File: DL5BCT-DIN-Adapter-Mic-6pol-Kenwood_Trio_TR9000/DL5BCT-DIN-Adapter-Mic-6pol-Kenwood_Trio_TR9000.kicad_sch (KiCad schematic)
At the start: 3 parts, among them J1 DIN-5_180degree, J2 GX16-6_Radio_Microphone-6-pol, J3 3.5 mm Audio Plug

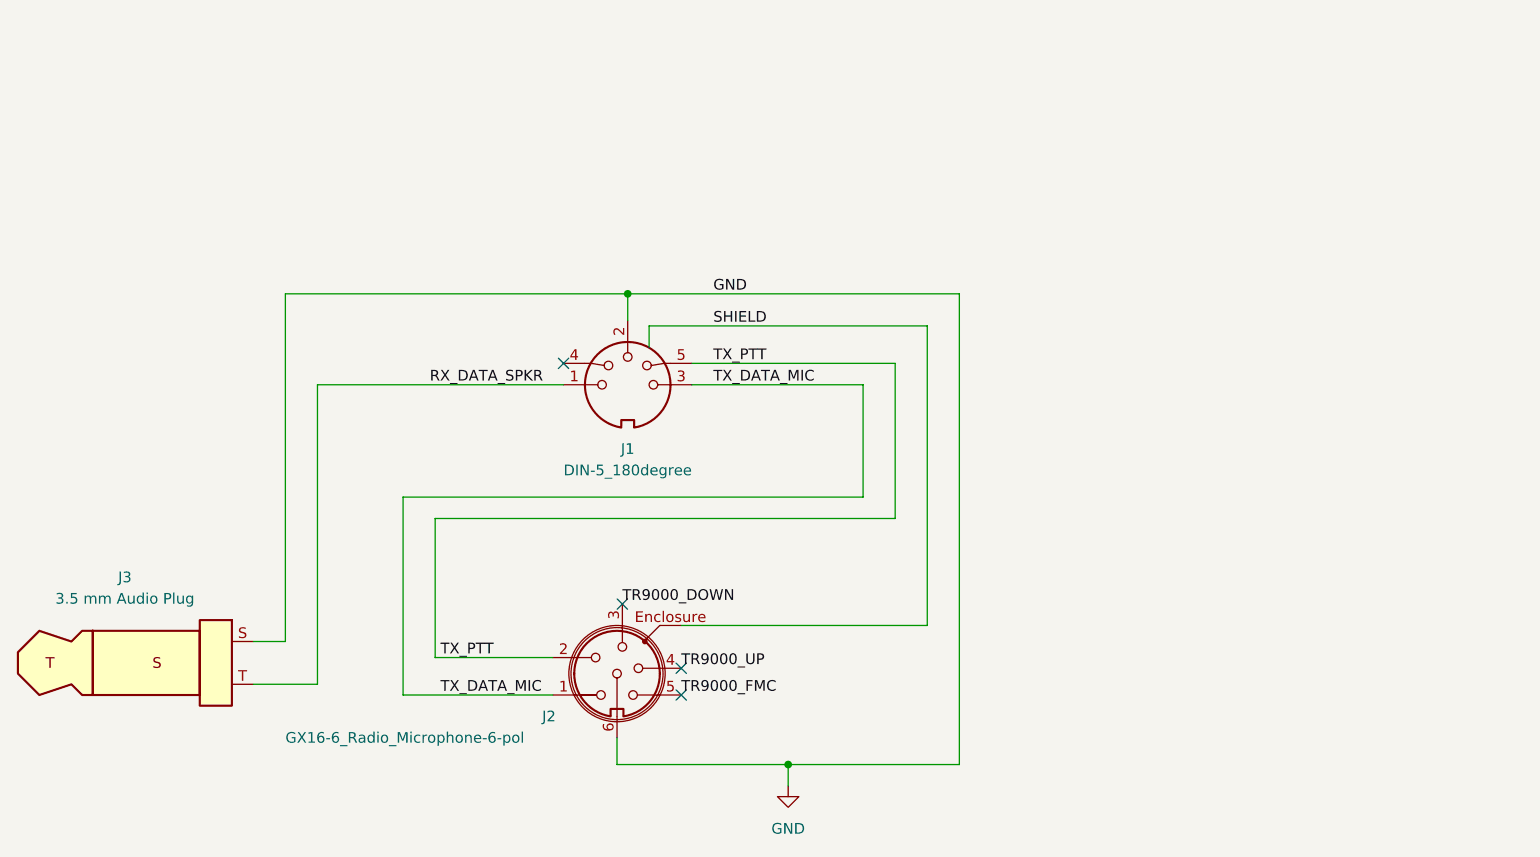
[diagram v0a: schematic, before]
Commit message: Added 'text table' with cable colour conventions. 	modified:   DL5BCT-DIN-Adapter-Mic-4pol-Sommerkamp_FT-277E/DL5BCT-DIN-Adapter-Mic-4pol-Sommerkamp_FT-277E.kicad_sch 	modified:   DL5BCT-DIN-Adapter-Mic-6pol-Kenwood_Trio_TR9000/DL5BCT-DIN-Adapter-Mic-6pol-Kenwood_Trio_TR9000.kicad_sch 	modified:   DL5BCT-DIN-Standard/DL5BCT-DIN-Standard.kicad_sch
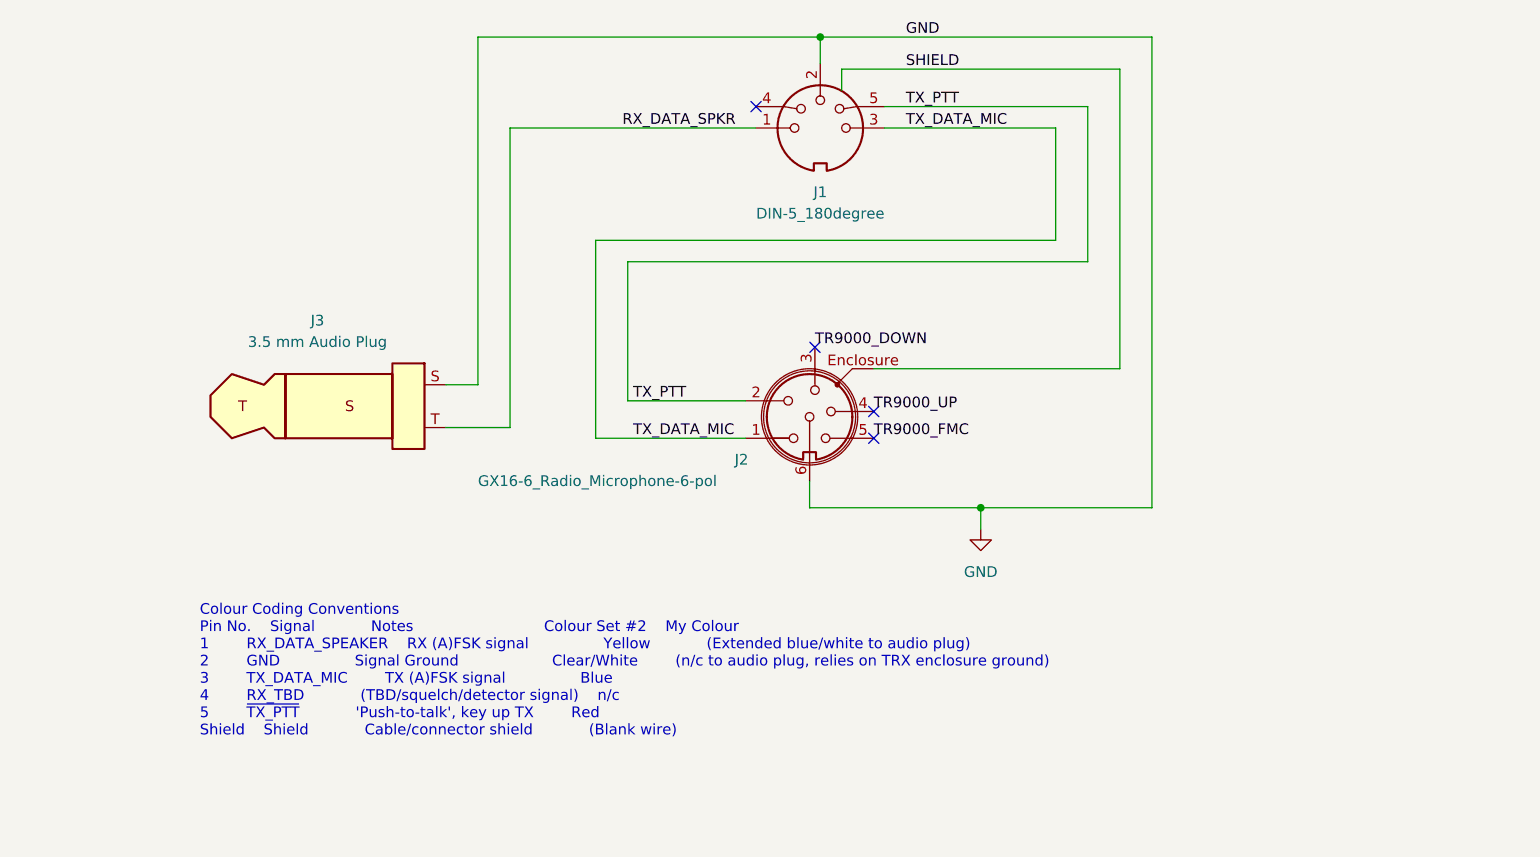
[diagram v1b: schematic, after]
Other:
- note added: "Colour Coding Conventions Pin No. Signal Notes Colour Set #2 My Colour 1 RX_DATA_SPEAKER RX (A)FSK signal Yellow (Extended blue/white to audio plug) 2 GND Signal Ground Clear/White (n/c to audio plug, relies on TRX enclosure ground) 3 TX_DATA_MIC TX (A)FSK signal Blue 4 RX_TBD (TBD/squelch/detector signal) n/c 5 ~{TX_PTT} 'Push-to-talk', key up TX Red Shield Shield Cable/connector shield (Blank w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"
- moved on the sheet: J1, J2, J3
